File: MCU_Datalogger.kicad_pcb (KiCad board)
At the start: 4 copper layers, 50.5 x 29.9 mm, 29 parts, among them J1 Conn_01x04_Pin, J2 Conn_01x09_Pin, J3 Conn_01x04_Pin, J4 Conn_02x03_Odd_Even, U1 DS1337S+, U2 24LC1025, U3 24LC1025, U4 ATMEGA328P-AU, Y1 32.768 KHz, Y2 16 MHz

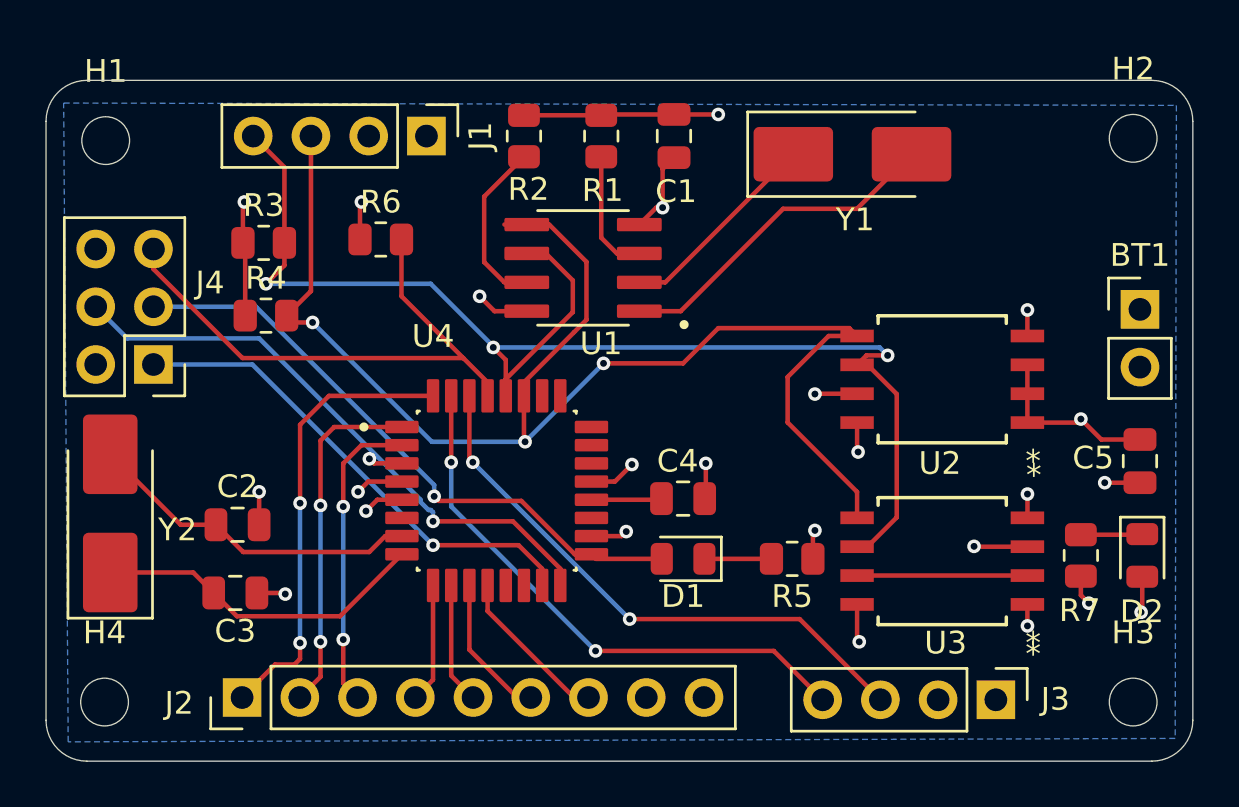
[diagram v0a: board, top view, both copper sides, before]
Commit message: changed the location of the clock and added silkscreen
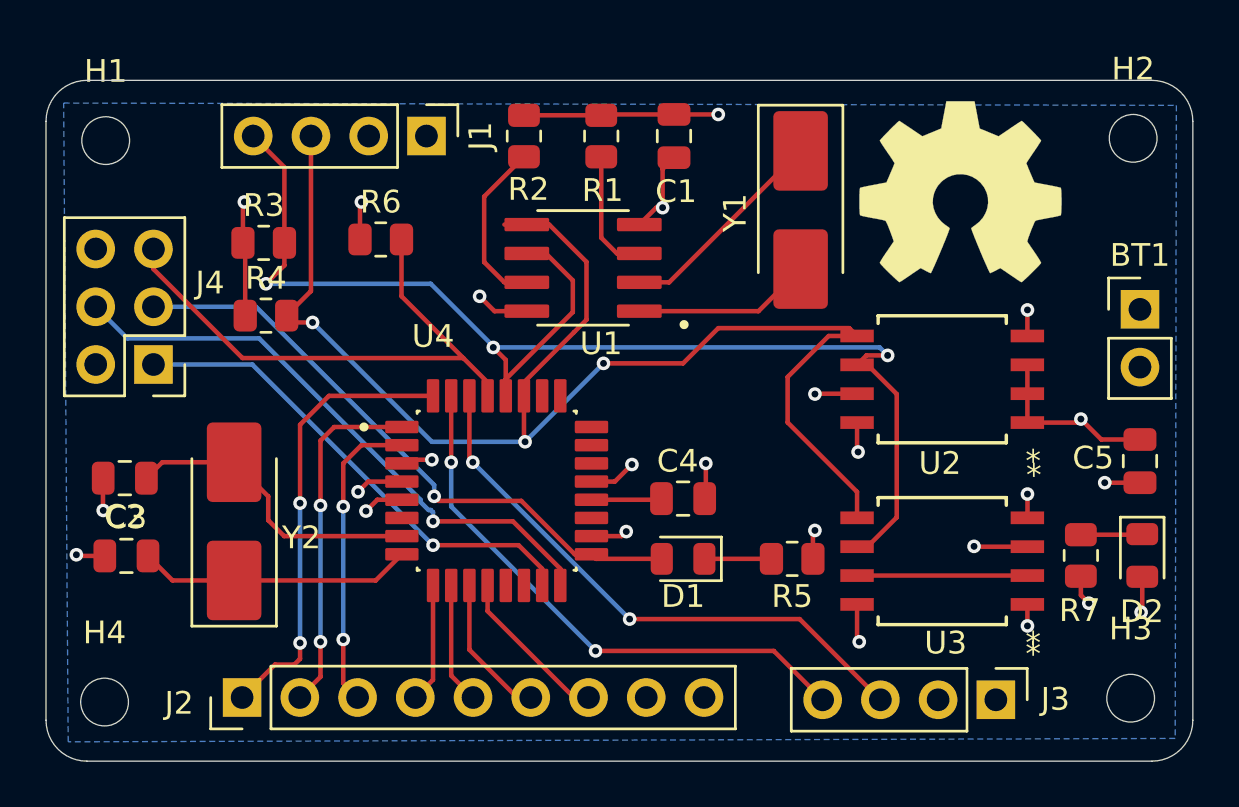
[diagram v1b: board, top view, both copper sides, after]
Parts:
- added REF**: OSHW-Symbol_8.9x8mm_SilkScreen, Symbol:OSHW-Symbol_8.9x8mm_SilkScreen, F.Cu at (75.6, 65.6)
- moved Y2 5.46 mm to (43.6, 80.0)
- moved C2 5.37 mm to (38.8, 78.2), turned to 180 degrees
- moved C3 5.06 mm to (38.9, 81.6), turned to 0 degrees
- moved Y1 3.35 mm to (68.6, 66.4), turned to -90 degrees
- moved H3 0.20 mm to (83.1, 87.8)
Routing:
- net Net-(U1-X1): track 14.8 -> 7.86 mm
- net Net-(U4-PB7): track 14.8 -> 12.1 mm
- net Net-(U4-PB6): track 14.9 -> 13.5 mm

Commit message: Bringed decoupling closer to processor
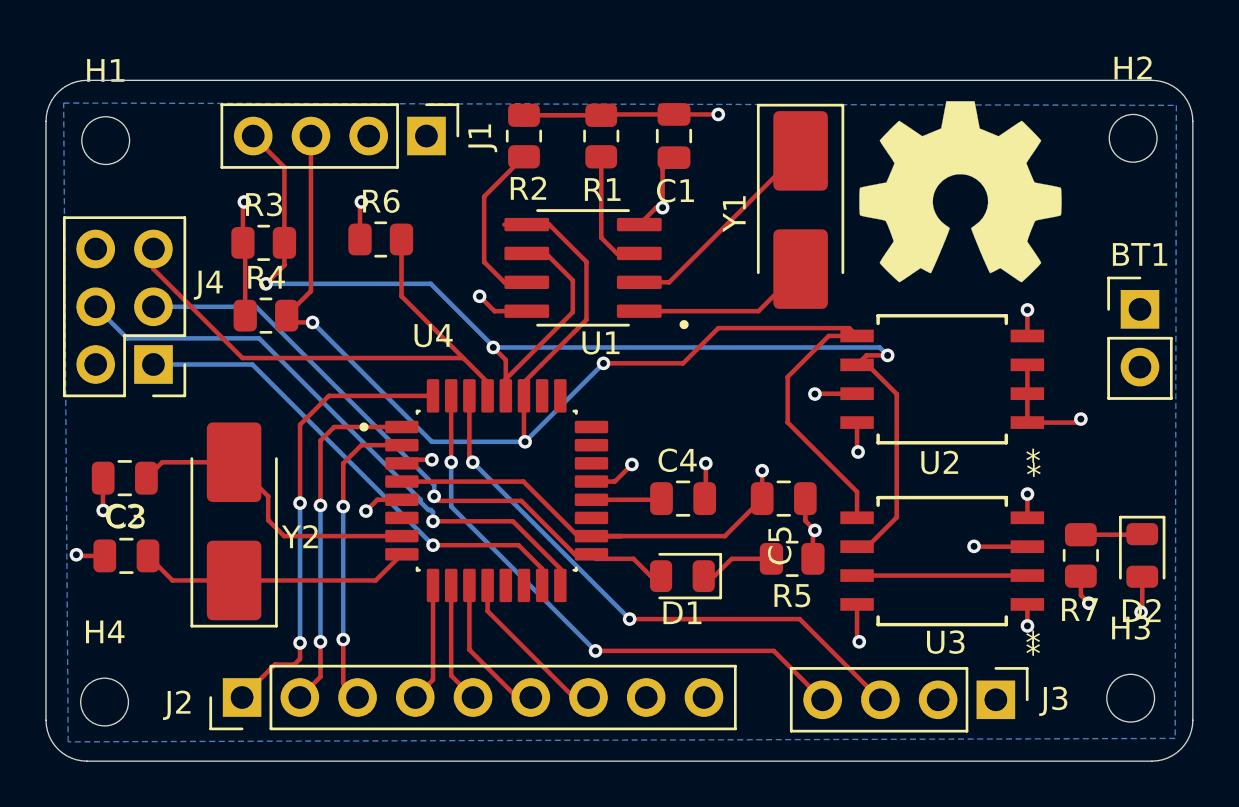
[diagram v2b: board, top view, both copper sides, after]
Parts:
- moved C5 15.8 mm to (67.8, 79.0), turned to 0 degrees
- moved D1 0.76 mm to (63.4, 82.5)
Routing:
- net /Vcc: track 37.0 -> 50.4 mm, vias 12 -> 11
- net GND: track 21.1 -> 21.2 mm, vias 13 -> 12
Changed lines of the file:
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@@
 	(footprint "LED_SMD:LED_0805_2012Metric"
 		(layer "F.Cu")
-		(at 63.4 81.7 180)
+		(at 63.37 82.46 180)
 		(descr "LED SMD 0805 (2012 Metric), square (rectangular) end terminal, IPC-7351 nominal, (Body size source: https://docs.google.com/spreadsheets/d/1BsfQQcO9C6DZCsRaXUlFlo91Tg2WpOkGARC1WS5S8t0/edit?usp=sharing)")
 		(tags "LED")
@@
 	(footprint "Capacitor_SMD:C_0805_2012Metric"
 		(layer "F.Cu")
-		(at 83.5 77.4 -90)
+		(at 67.83 79.05)
 		(descr "Capacitor SMD 0805 (2012 Metric), square (rectangular) end terminal, IPC-7351 nominal, (Body size source: IPC-SM-782 page 76, https://www.pcb-3d.com/wordpress/wp-content/uploads/ipc-sm-782a_amendment_1_and_2.pdf, https://docs.google.com/spreadsheets/d/1BsfQQcO9C6DZCsRaXUlFlo91Tg2WpOkGARC1WS5S8t0/edit?usp=sharing)")
 		(tags "capacitor")
 		(property "Reference" "C5"
-			(at -0.14 2.06 180)
+			(at -0.14 2.06 90)
 			(layer "F.SilkS")
 			(effects
@@
 		)
 		(property "Value" "100 nF"
-			(at 0 1.68 90)
+			(at 0 1.68 0)
 			(layer "F.Fab")
 			(effects
@@
 		)
 		(property "Datasheet" ""
-			(at 0 0 90)
+			(at 0 0 0)
 			(layer "F.Fab")
 			(hide yes)
@@
 		)
 		(property "Description" "Polarized capacitor"
-			(at 0 0 90)
+			(at 0 0 0)
 			(layer "F.Fab")
 			(hide yes)
@@
 		)
 		(property "KiLib_Generator" "SMD_2terminal_chip_molded"
-			(at 0 0 90)
+			(at 0 0 0)
 			(layer "F.SilkS")
 			(hide yes)
@@
 		(duplicate_pad_numbers_are_jumpers no)
 		(fp_line
-			(start -0.261252 0.735)
-			(end 0.261252 0.735)
+			(start -0.261252 -0.735)
+			(end 0.261252 -0.735)
 			(stroke
 				(width 0.12)
@@
 		)
 		(fp_line
-			(start -0.261252 -0.735)
-			(end 0.261252 -0.735)
+			(start -0.261252 0.735)
+			(end 0.261252 0.735)
 			(stroke
 				(width 0.12)
@@
 		)
 		(fp_text user "${REFERENCE}"
-			(at 0 0 90)
+			(at 0 0 0)
 			(layer "F.Fab")
 			(effects
@@
 		)
 		(pad "1" smd roundrect
-			(at -0.95 0 270)
+			(at -0.95 0)
 			(size 1 1.45)
 			(layers "F.Cu" "F.Mask" "F.Paste")
@@
 		)
 		(pad "2" smd roundrect
-			(at 0.95 0 270)
+			(at 0.95 0)
 			(size 1 1.45)
 			(layers "F.Cu" "F.Mask" "F.Paste")
@@
 	)
 	(segment
-		(start 61.475 66.995)
-		(end 62.22 66.25)
+		(start 68.78 80.03)
+		(end 69.2 80.45)
 		(width 0.2)
 		(layer "F.Cu")
@@
 	)
 	(segment
-		(start 52.35 77.34)
-		(end 51.19 77.34)
+		(start 61.475 66.995)
+		(end 62.22 66.25)
 		(width 0.2)
 		(layer "F.Cu")
@@
 	)
 	(segment
-		(start 83.5 78.35)
-		(end 82 78.35)
+		(start 52.35 77.34)
+		(end 51.19 77.34)
 		(width 0.2)
 		(layer "F.Cu")
@@
 	)
 	(segment
+		(start 68.78 79.05)
+		(end 68.78 80.03)
+		(width 0.2)
+		(layer "F.Cu")
+		(net "GND")
+	)
+	(segment
 		(start 64.4 77.5)
 		(end 64.4 79)
@@
 	)
 	(via
-		(at 81.95 78.35)
-		(size 0.6)
-		(drill 0.3)
-		(layers "F.Cu" "B.Cu")
-		(net "GND")
-	)
-	(via
 		(at 49.45 79.6)
 		(size 0.6)
@@
 	)
 	(segment
-		(start 60.7 80.7)
-		(end 60.9 80.5)
-		(width 0.2)
-		(layer "F.Cu")
-		(net "/Vcc")
-	)
-	(segment
 		(start 44.0375 67.8)
 		(end 44.0375 66.0625)
@@
 	)
 	(segment
-		(start 81.8 76.45)
-		(end 80.9 75.55)
-		(width 0.2)
-		(layer "F.Cu")
-		(net "/Vcc")
-	)
-	(segment
 		(start 63 62.15)
 		(end 64.8 62.15)
@@
 	)
 	(segment
-		(start 51.03 78.3)
-		(end 49.55 78.3)
+		(start 78.5465 75.705)
+		(end 80.745 75.705)
 		(width 0.2)
 		(layer "F.Cu")
@@
 	)
 	(segment
-		(start 78.5465 75.705)
-		(end 80.745 75.705)
+		(start 59.37 80.7)
+		(end 65.24 80.7)
+		(width 0.2)
+		(layer "F.Cu")
+		(net "/Vcc")
+	)
+	(segment
+		(start 56.374104 78.3)
+		(end 58.774104 80.7)
 		(width 0.2)
 		(layer "F.Cu")
@@
 	)
 	(segment
-		(start 49.55 78.3)
-		(end 49.1 78.75)
+		(start 65.24 80.7)
+		(end 66.88 79.06)
 		(width 0.2)
 		(layer "F.Cu")
@@
 	)
 	(segment
-		(start 71.0535 75.705)
-		(end 71.0535 76.9535)
+		(start 51.03 78.3)
+		(end 56.374104 78.3)
 		(width 0.2)
 		(layer "F.Cu")
@@
 	)
 	(segment
-		(start 83.5 76.45)
-		(end 81.8 76.45)
+		(start 71.0535 75.705)
+		(end 71.0535 76.9535)
 		(width 0.2)
 		(layer "F.Cu")
@@
 	)
 	(segment
+		(start 58.774104 80.7)
+		(end 59.37 80.7)
+		(width 0.2)
+		(layer "F.Cu")
+		(net "/Vcc")
+	)
+	(segment
 		(start 59.8375 62.15)
 		(end 59.8 62.1875)
@@
 	)
 	(segment
+		(start 66.88 79.05)
+		(end 66.88 77.82)
+		(width 0.2)
+		(layer "F.Cu")
+		(net "/Vcc")
+	)
+	(segment
+		(start 66.88 79.06)
+		(end 66.88 79.05)
+		(width 0.2)
+		(layer "F.Cu")
+		(net "/Vcc")
+	)
+	(segment
 		(start 83.6 84)
 		(end 83.55 84.05)
@@
 	)
 	(via
+		(at 66.88 77.82)
+		(size 0.6)
+		(drill 0.3)
+		(layers "F.Cu" "B.Cu")
+		(net "/Vcc")
+	)
+	(via
 		(at 71.1 77)
 		(size 0.6)
@@
 	)
 	(via
-		(at 49.1 78.75)
-		(size 0.6)
-		(drill 0.3)
-		(layers "F.Cu" "B.Cu")
-		(free yes)
-		(net "/Vcc")
-	)
-	(via
 		(at 71.15 85.35)
 		(size 0.6)
@@
 		(net "/Vcc")
 	)
-	(via
-		(at 60.9 80.5)
-		(size 0.6)
-		(drill 0.3)
-		(layers "F.Cu" "B.Cu")
-		(net "/Vcc")
-	)
 	(segment
 		(start 39.79 78.15)
@@
 	)
 	(segment
-		(start 59.57 81.7)
-		(end 59.37 81.5)
-		(width 0.2)
-		(layer "F.Cu")
-		(net "/SCK")
-	)
-	(segment
-		(start 62.4625 81.7)
+		(start 61.2225 81.7)
 		(end 59.57 81.7)
 		(width 0.2)
@@
 	)
 	(segment
+		(start 62.4325 82.46)
+		(end 61.9825 82.46)
+		(width 0.2)
+		(layer "F.Cu")
+		(net "/SCK")
+	)
+	(segment
+		(start 59.57 81.7)
+		(end 59.37 81.5)
+		(width 0.2)
+		(layer "F.Cu")
+		(net "/SCK")
+	)
+	(segment
 		(start 56.285 79.15)
 		(end 58.635 81.5)
@@
 		(net "/SCK")
 	)
+	(segment
+		(start 61.9825 82.46)
+		(end 61.2225 81.7)
+		(width 0.2)
+		(layer "F.Cu")
+		(net "/SCK")
+	)
 	(via
 		(at 52.449265 78.950735)
@@
 	)
 	(segment
-		(start 64.3375 81.7)
+		(start 65.5375 81.7)
 		(end 67.2875 81.7)
 		(width 0.2)
 		(layer "F.Cu")
+		(net "Net-(D1-K)")
+	)
+	(segment
+		(start 64.7775 82.46)
+		(end 65.5375 81.7)
+		(width 0.2)
+		(layer "F.Cu")
+		(net "Net-(D1-K)")
+	)
+	(segment
+		(start 64.3075 82.46)
+		(end 64.7775 82.46)
+		(width 0.2)
+		(layer "F.Cu")
